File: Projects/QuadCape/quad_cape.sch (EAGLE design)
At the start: 9 parts, among them U1 ADXL345, U2 ITG-3200, U3 LS20031

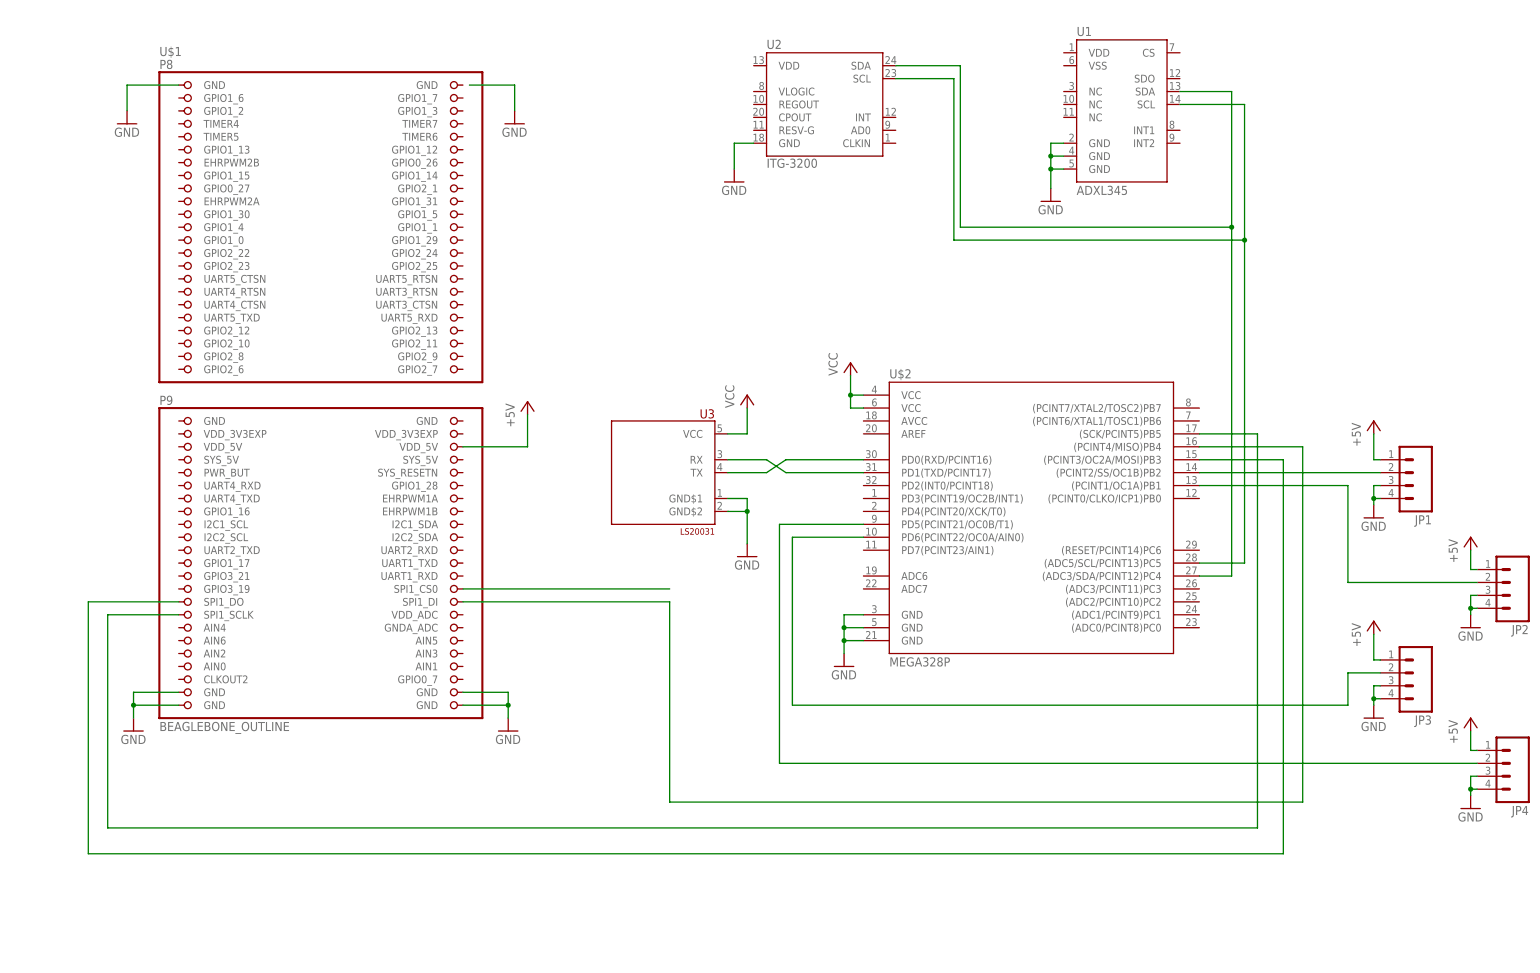
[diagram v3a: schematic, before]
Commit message: Replaced individual Compass and Gyro with Sparkfun 6DOF-Digital module
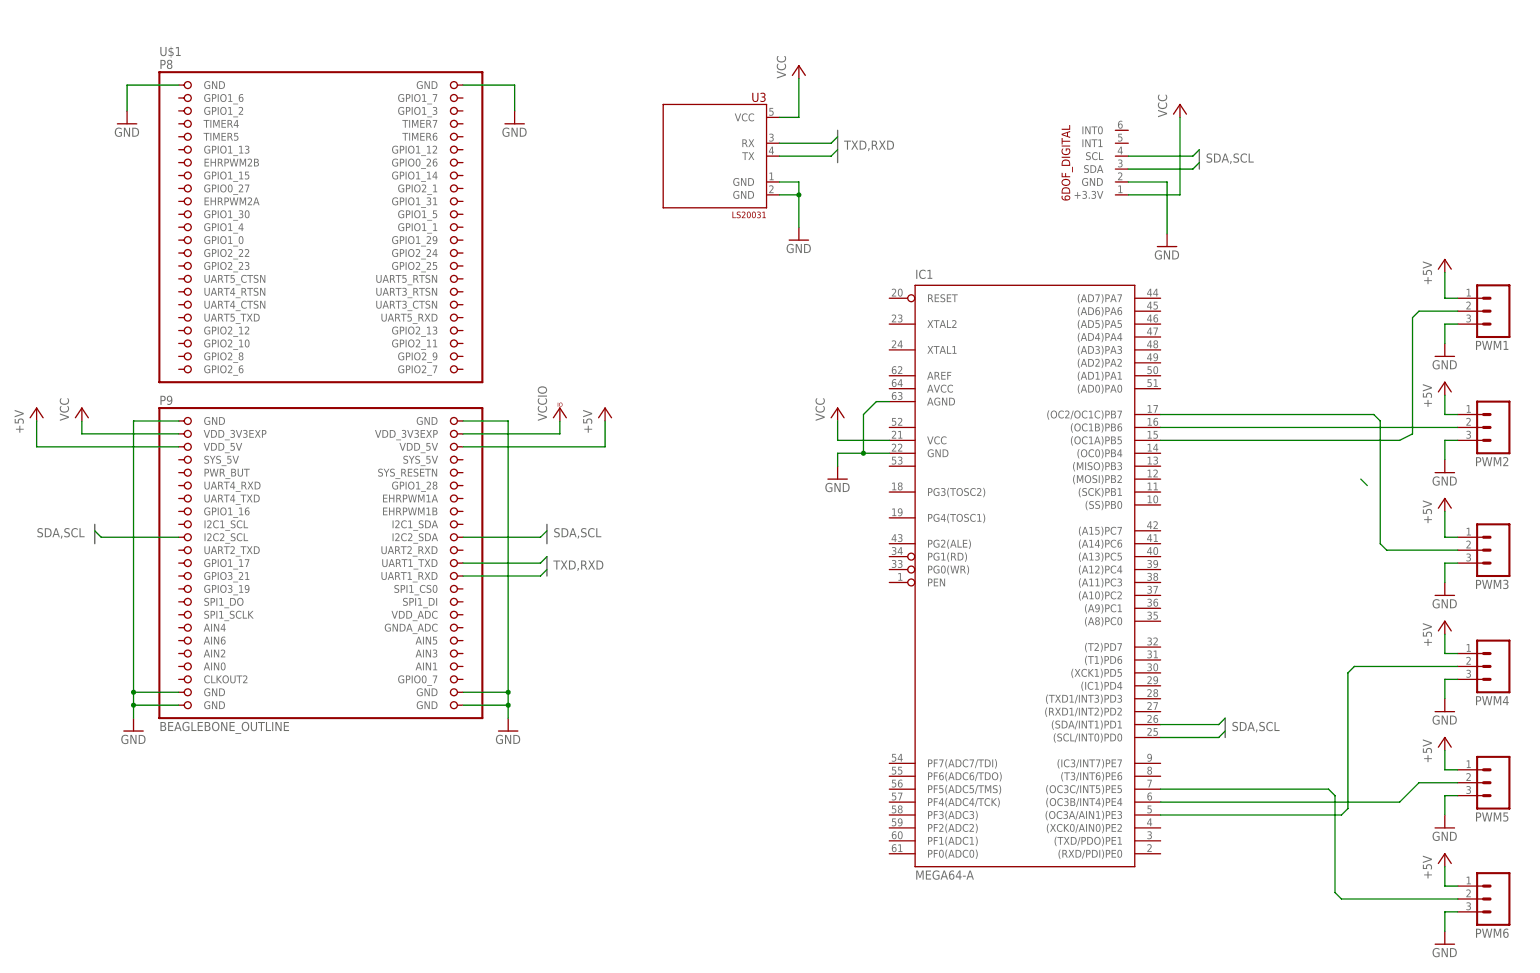
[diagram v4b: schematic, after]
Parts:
- removed JP1, JP2, JP3, JP4: (no value), SparkFun-Connectors:M04PTH
- removed U1: ADXL345, SparkFun-Sensors:ADXL345
- removed U2: ITG-3200, SparkFun-Sensors:ITG-3200
- added IC1: MEGA64-A, avr:MEGA64-A
- added PWM1, PWM2, PWM3, PWM4, PWM5, PWM6: (no value), SparkFun-Connectors:M03
- U$2: value MEGA328P -> 6DOF-DIGITAL; device custom:MEGA328P -> SparkFun-Breakouts:6DOF-DIGITAL
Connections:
- removed net N$1: U$2.PD0(RXD/PCINT16), U3.TX
- removed net N$11: U$1.SPI1_CS0
- removed net N$12: JP4.2, U$2.PD5(PCINT21/OC0B/T1)
- removed net N$15: U$1.SPI1_SCLK, U$2.(SCK/PCINT5)PB5
- removed net N$2: U$2.PD1(TXD/PCINT17), U3.RX
- removed net N$3: U$1.SPI1_DO, U$2.(PCINT3/OC2A/MOSI)PB3
- removed net N$4: JP2.2, U$2.(PCINT1/OC1A)PB1
- removed net N$5: JP3.2, U$2.PD6(PCINT22/OC0A/AIN0)
- removed net N$6: U$1.SPI1_DI, U$2.(PCINT4/MISO)PB4
- removed net N$7: U$2.(ADC3/SDA/PCINT12)PC4, U1.SDA, U2.SDA
- removed net N$8: U$2.(ADC5/SCL/PCINT13)PC5, U1.SCL, U2.SCL
- removed net N$9: JP1.2, U$2.(PCINT2/SS/OC1B)PB2
- new net PWM1: IC1.(OC1A)PB5, PWM1.2
- new net PWM2: IC1.(OC1B)PB6, PWM2.2
- new net PWM3: IC1.(OC2/OC1C)PB7, PWM3.2
- new net PWM4: IC1.(OC3A/AIN1)PE3, PWM4.2
- new net PWM5: IC1.(OC3B/INT4)PE4, PWM5.2
- new net PWM6: IC1.(OC3C/INT5)PE5, PWM6.2
- new net RXD: U$1.UART1_RXD, U3.TX
- new net SCL: IC1.(SCL/INT0)PD0, U$1.I2C2_SCL, U$2.SCL
- new net SDA: IC1.(SDA/INT1)PD1, U$1.I2C2_SDA, U$2.SDA
- new net TXD: U$1.UART1_TXD, U3.RX
- new net VCCIO: U$1.VDD_3V3EXP@2
- net +5V: now also PWM1.1, PWM2.1, PWM3.1, PWM4.1, PWM5.1, PWM6.1, U$1.VDD_5V@1; no longer JP1.1, JP2.1, JP3.1, JP4.1
- net GND: now also IC1.AGND, IC1.GND, PWM1.3, PWM2.3, PWM3.3, PWM4.3, PWM5.3, PWM6.3, U$1.GND@1, U$1.GND@2, U$1.GND@8, U$2.GND, U3.GND@1, U3.GND@2; no longer JP1.3, JP1.4, JP2.3, JP2.4, JP3.3, JP3.4, JP4.3, JP4.4, U$2.GND@1, U$2.GND@2, U$2.GND@3, U1.GND@2, U1.GND@4, U1.GND@5, U2.GND, U3.GND$1, U3.GND$2
- net VCC: now also IC1.VCC, U$1.VDD_3V3EXP@1, U$2.+3.3V; no longer U$2.VCC@1, U$2.VCC@2
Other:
- moved on the sheet: U3
